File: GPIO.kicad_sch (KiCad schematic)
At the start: 18 parts

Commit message: Notes in kicad's sheet text blocks
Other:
- company: (none) -> Logic Systems Int'l Inc
- title: (none) -> CEDA - Sanco 8003 schematics
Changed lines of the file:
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@@
 (kicad_sch (version 20230121) (generator eeschema)
   (paper "A4")
+  (title_block
+    (title "CEDA - Sanco 8003 schematics")
+    (rev "05")
+    (company "Logic Systems Int'l Inc")
+    (comment 1 "reversed by RetrOfficina - retrofficina.glgprograms.it")
+    (comment 2 "control and for parallel port")
+    (comment 3 "The uPD8255 PIO is used for multiple purposes, including bank switching, peripheral")
+    (comment 4 "GPIO")
+  )
   (junction (at 142.24 95.25) (diameter 0) (color 0 0 0 0)
   )

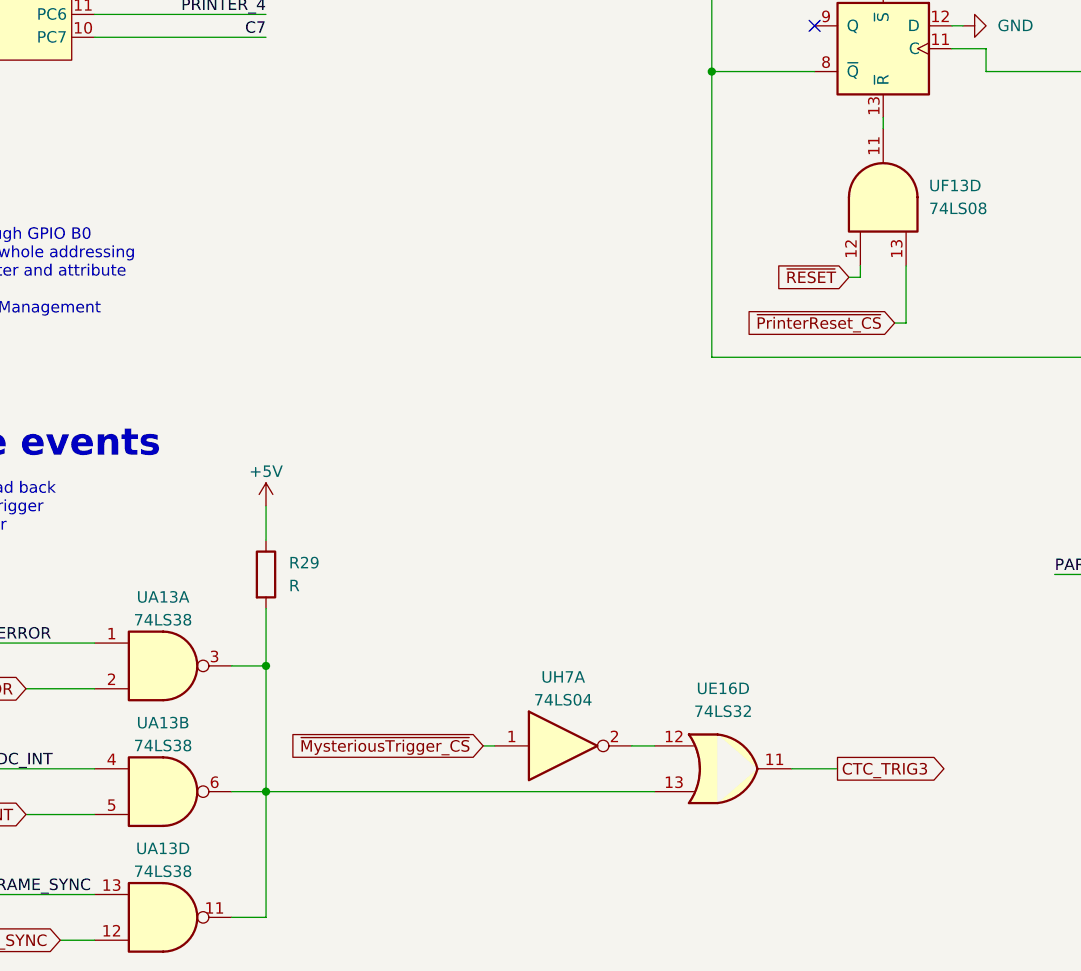
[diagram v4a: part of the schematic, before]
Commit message: Upgrade to KiCAD 9.0
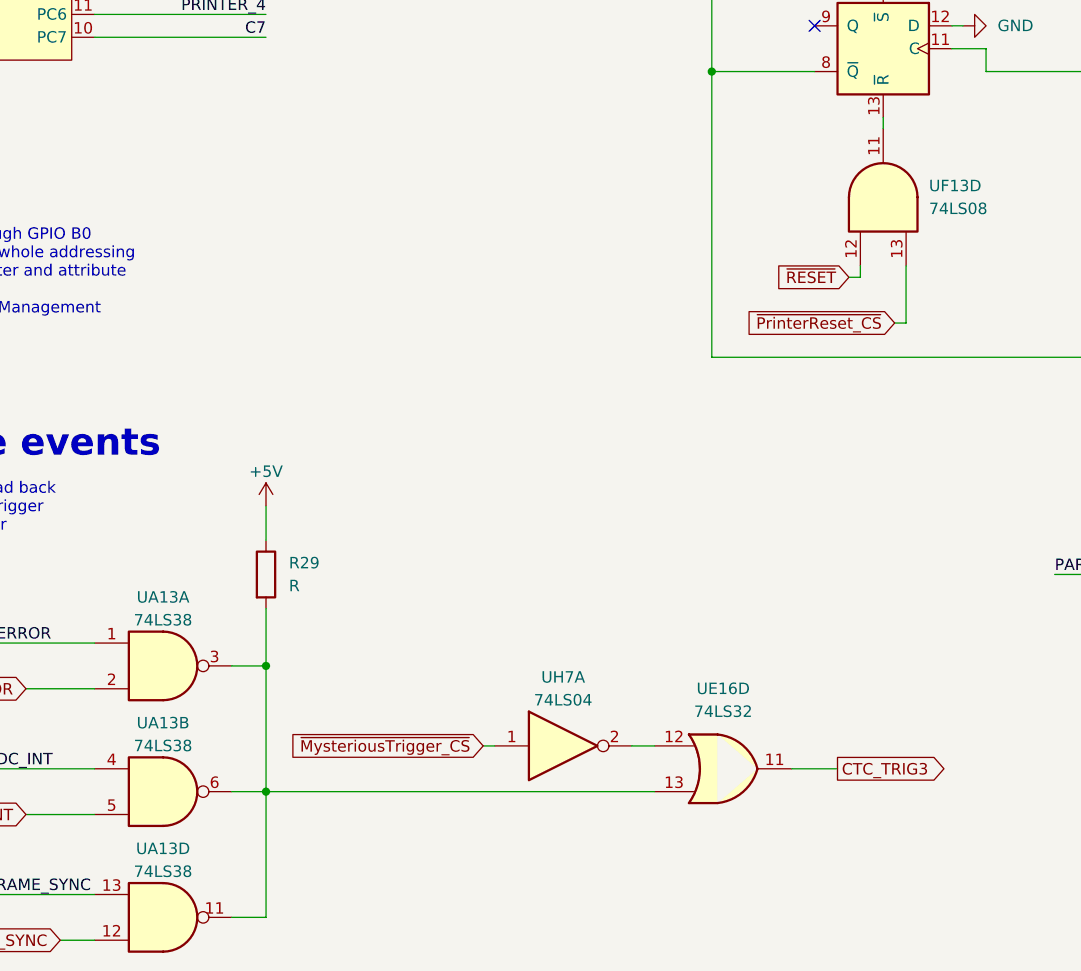
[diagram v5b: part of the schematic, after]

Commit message: Assigned default footprints to ICs
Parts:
- UA10: footprint (none) -> Package_DIP:DIP-20_W7.62mm
- UA13, UB2, UB8, UE16, UF13, UH7: footprint (none) -> Package_DIP:DIP-14_W7.62mm
- UB10: footprint (none) -> Package_DIP:DIP-40_W15.24mm
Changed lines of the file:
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@@
 			)
 		)
-		(property "Footprint" ""
+		(property "Footprint" "Package_DIP:DIP-14_W7.62mm"
 			(at 143.51 172.72 0)
 			(effects
@@
 			)
 		)
-		(property "Footprint" ""
+		(property "Footprint" "Package_DIP:DIP-14_W7.62mm"
 			(at 161.29 92.71 0)
 			(effects
@@
 			)
 		)
-		(property "Footprint" ""
+		(property "Footprint" "Package_DIP:DIP-14_W7.62mm"
 			(at 196.85 92.71 0)
 			(effects
@@
 			)
 		)
-		(property "Footprint" ""
+		(property "Footprint" "Package_DIP:DIP-14_W7.62mm"
 			(at 198.12 151.13 0)
 			(effects
@@
 			)
 		)
-		(property "Footprint" ""
+		(property "Footprint" "Package_DIP:DIP-14_W7.62mm"
 			(at 198.12 127 0)
 			(effects
@@
 			)
 		)
-		(property "Footprint" ""
+		(property "Footprint" "Package_DIP:DIP-14_W7.62mm"
 			(at 81.28 161.29 0)
 			(effects
@@
 			)
 		)
-		(property "Footprint" ""
+		(property "Footprint" "Package_DIP:DIP-14_W7.62mm"
 			(at 81.28 189.23 0)
 			(effects
@@
 			)
 		)
-		(property "Footprint" ""
+		(property "Footprint" "Package_DIP:DIP-40_W15.24mm"
 			(at 50.165 66.04 0)
 			(effects
@@
 			)
 		)
-		(property "Footprint" ""
+		(property "Footprint" "Package_DIP:DIP-14_W7.62mm"
 			(at 125.73 170.18 0)
 			(effects
@@
 			)
 		)
-		(property "Footprint" ""
+		(property "Footprint" "Package_DIP:DIP-20_W7.62mm"
 			(at 201.93 48.26 0)
 			(effects
@@
 			)
 		)
-		(property "Footprint" ""
+		(property "Footprint" "Package_DIP:DIP-14_W7.62mm"
 			(at 161.29 109.22 0)
 			(effects
@@
 			)
 		)
-		(property "Footprint" ""
+		(property "Footprint" "Package_DIP:DIP-14_W7.62mm"
 			(at 81.28 175.26 0)
 			(effects

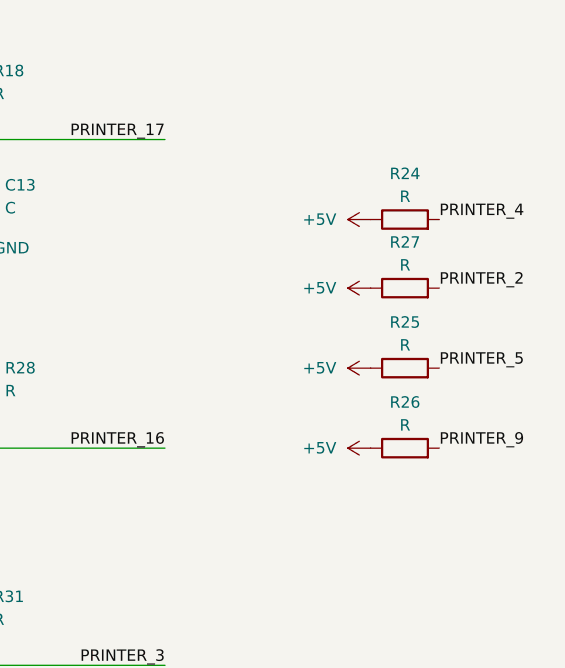
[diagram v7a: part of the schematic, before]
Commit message: pcb: added and placed almost all components
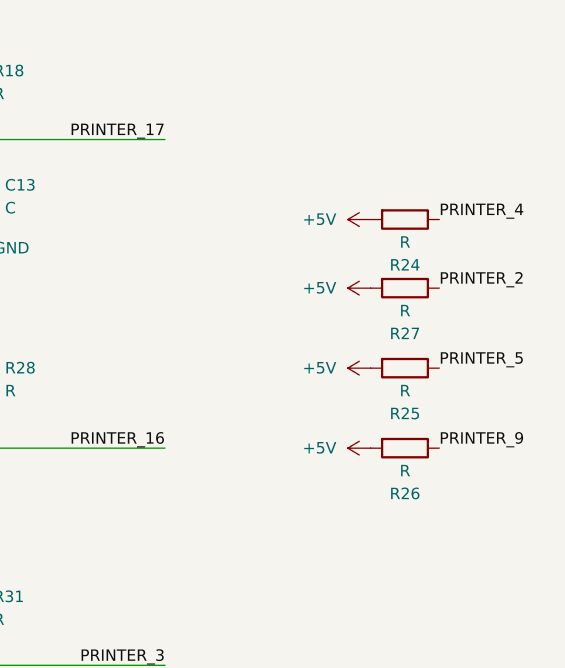
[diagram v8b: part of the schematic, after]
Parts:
- C13: footprint (none) -> Capacitor_THT:C_Disc_D4.3mm_W1.9mm_P5.00mm
- R18, R24, R25, R26, R27, R28, R29, R31: footprint (none) -> Resistor_THT:R_Axial_DIN0204_L3.6mm_D1.6mm_P5.08mm_Vertical
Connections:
- net +5V: now also R24.2, R25.2, R26.2, R27.2; no longer R24.1, R25.1, R26.1, R27.1
- net PRINTER_2: now also R27.1; no longer R27.2
- net PRINTER_4: now also R24.1; no longer R24.2
- net PRINTER_5: now also R25.1; no longer R25.2
- net PRINTER_9: now also R26.1; no longer R26.2
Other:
- moved on the sheet: R24, R25, R26, R27
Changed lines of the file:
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@@
 			)
 		)
-		(property "Footprint" ""
+		(property "Footprint" "Resistor_THT:R_Axial_DIN0204_L3.6mm_D1.6mm_P5.08mm_Vertical"
 			(at 217.678 86.36 90)
 			(effects
@@
 			)
 		)
-		(property "Footprint" ""
+		(property "Footprint" "Resistor_THT:R_Axial_DIN0204_L3.6mm_D1.6mm_P5.08mm_Vertical"
 			(at 217.678 119.38 90)
 			(effects
@@
 	(symbol
 		(lib_id "Device:R")
-		(at 264.16 127 90)
+		(at 264.16 127 270)
 		(unit 1)
 		(exclude_from_sim no)
@@
 		(dnp no)
 		(property "Reference" "R26"
-			(at 264.16 121.92 90)
+			(at 264.16 132.08 90)
 			(effects
 				(font
@@
 		)
 		(property "Value" "R"
-			(at 264.16 124.46 90)
-			(effects
-				(font
-					(size 1.27 1.27)
-				)
-			)
-		)
-		(property "Footprint" ""
-			(at 264.16 128.778 90)
+			(at 264.16 129.54 90)
+			(effects
+				(font
+					(size 1.27 1.27)
+				)
+			)
+		)
+		(property "Footprint" "Resistor_THT:R_Axial_DIN0204_L3.6mm_D1.6mm_P5.08mm_Vertical"
+			(at 264.16 125.222 90)
 			(effects
 				(font
@@
 	(symbol
 		(lib_id "Device:R")
-		(at 264.16 109.22 90)
+		(at 264.16 109.22 270)
 		(unit 1)
 		(exclude_from_sim no)
@@
 		(dnp no)
 		(property "Reference" "R27"
-			(at 264.16 104.14 90)
+			(at 264.16 114.3 90)
 			(effects
 				(font
@@
 		)
 		(property "Value" "R"
-			(at 264.16 106.68 90)
-			(effects
-				(font
-					(size 1.27 1.27)
-				)
-			)
-		)
-		(property "Footprint" ""
-			(at 264.16 110.998 90)
+			(at 264.16 111.76 90)
+			(effects
+				(font
+					(size 1.27 1.27)
+				)
+			)
+		)
+		(property "Footprint" "Resistor_THT:R_Axial_DIN0204_L3.6mm_D1.6mm_P5.08mm_Vertical"
+			(at 264.16 107.442 90)
 			(effects
 				(font
@@
 			)
 		)
-		(property "Footprint" ""
+		(property "Footprint" "Resistor_THT:R_Axial_DIN0204_L3.6mm_D1.6mm_P5.08mm_Vertical"
 			(at 90.932 151.13 90)
 			(effects
@@
 			)
 		)
-		(property "Footprint" ""
+		(property "Footprint" "Resistor_THT:R_Axial_DIN0204_L3.6mm_D1.6mm_P5.08mm_Vertical"
 			(at 214.122 144.78 90)
 			(effects
@@
 	(symbol
 		(lib_id "Device:R")
-		(at 264.16 118.11 90)
+		(at 264.16 118.11 270)
 		(unit 1)
 		(exclude_from_sim no)
@@
 		(dnp no)
 		(property "Reference" "R25"
-			(at 264.16 113.03 90)
+			(at 264.16 123.19 90)
 			(effects
 				(font
@@
 		)
 		(property "Value" "R"
-			(at 264.16 115.57 90)
-			(effects
-				(font
-					(size 1.27 1.27)
-				)
-			)
-		)
-		(property "Footprint" ""
-			(at 264.16 119.888 90)
+			(at 264.16 120.65 90)
+			(effects
+				(font
+					(size 1.27 1.27)
+				)
+			)
+		)
+		(property "Footprint" "Resistor_THT:R_Axial_DIN0204_L3.6mm_D1.6mm_P5.08mm_Vertical"
+			(at 264.16 116.332 90)
 			(effects
 				(font
@@
 	(symbol
 		(lib_id "Device:R")
-		(at 264.16 101.6 90)
+		(at 264.16 101.6 270)
 		(unit 1)
 		(exclude_from_sim no)
@@
 		(dnp no)
 		(property "Reference" "R24"
-			(at 264.16 96.52 90)
+			(at 264.16 106.68 90)
 			(effects
 				(font
@@
 		)
 		(property "Value" "R"
-			(at 264.16 99.06 90)
-			(effects
-				(font
-					(size 1.27 1.27)
-				)
-			)
-		)
-		(property "Footprint" ""
-			(at 264.16 103.378 90)
+			(at 264.16 104.14 90)
+			(effects
+				(font
+					(size 1.27 1.27)
+				)
+			)
+		)
+		(property "Footprint" "Resistor_THT:R_Axial_DIN0204_L3.6mm_D1.6mm_P5.08mm_Vertical"
+			(at 264.16 99.822 90)
 			(effects
 				(font
@@
 			)
 		)
-		(property "Footprint" ""
+		(property "Footprint" "Capacitor_THT:C_Disc_D4.3mm_W1.9mm_P5.00mm"
 			(at 214.9348 102.87 0)
 			(effects
